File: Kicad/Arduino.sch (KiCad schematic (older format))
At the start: 5 parts

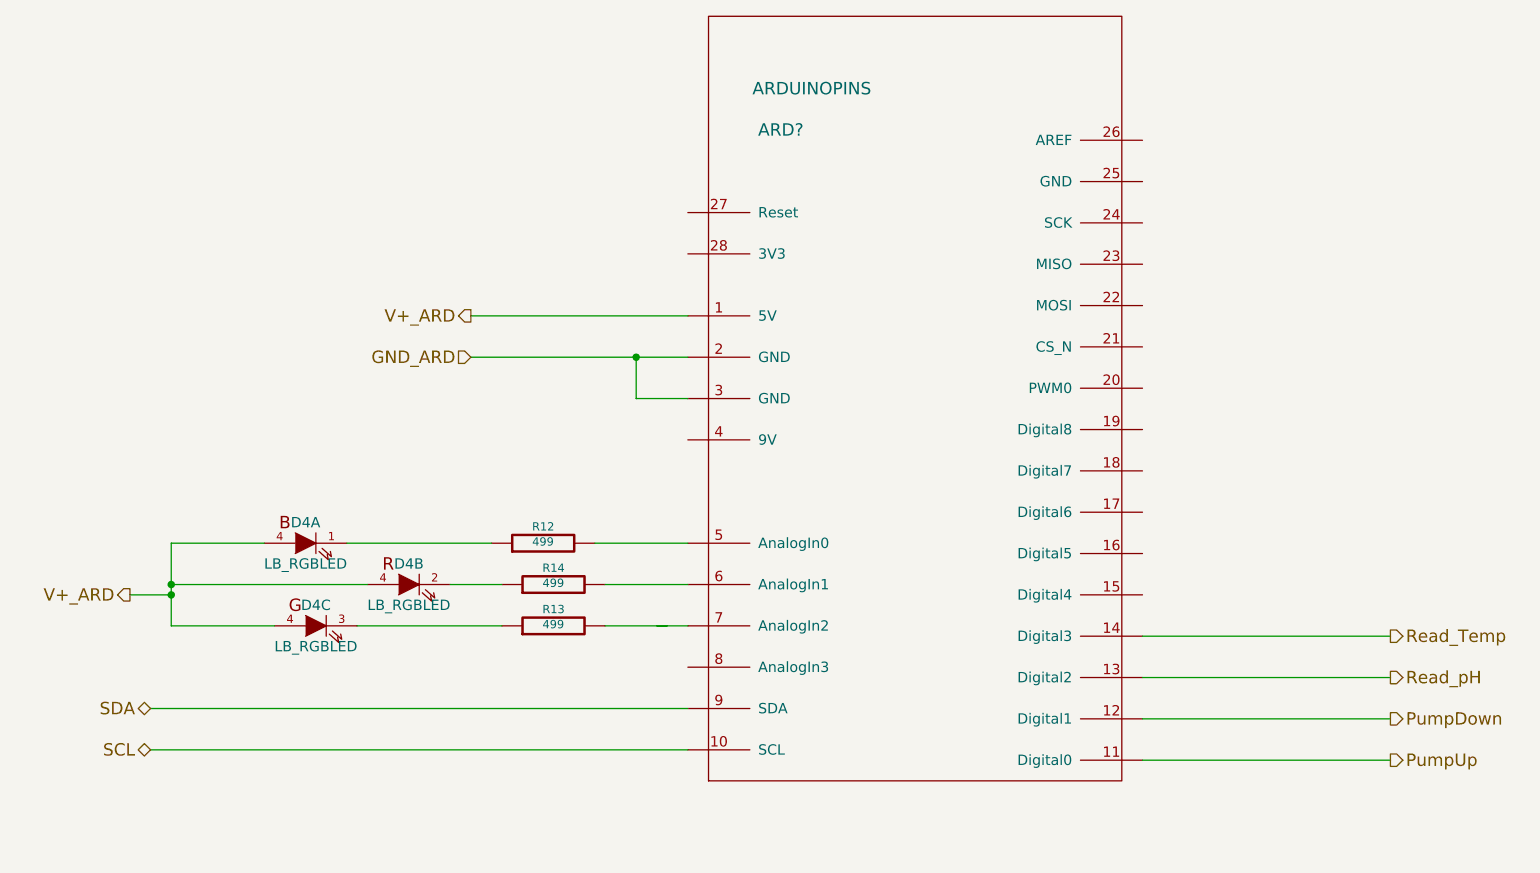
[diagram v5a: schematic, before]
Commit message: prior to using Arduino ADC
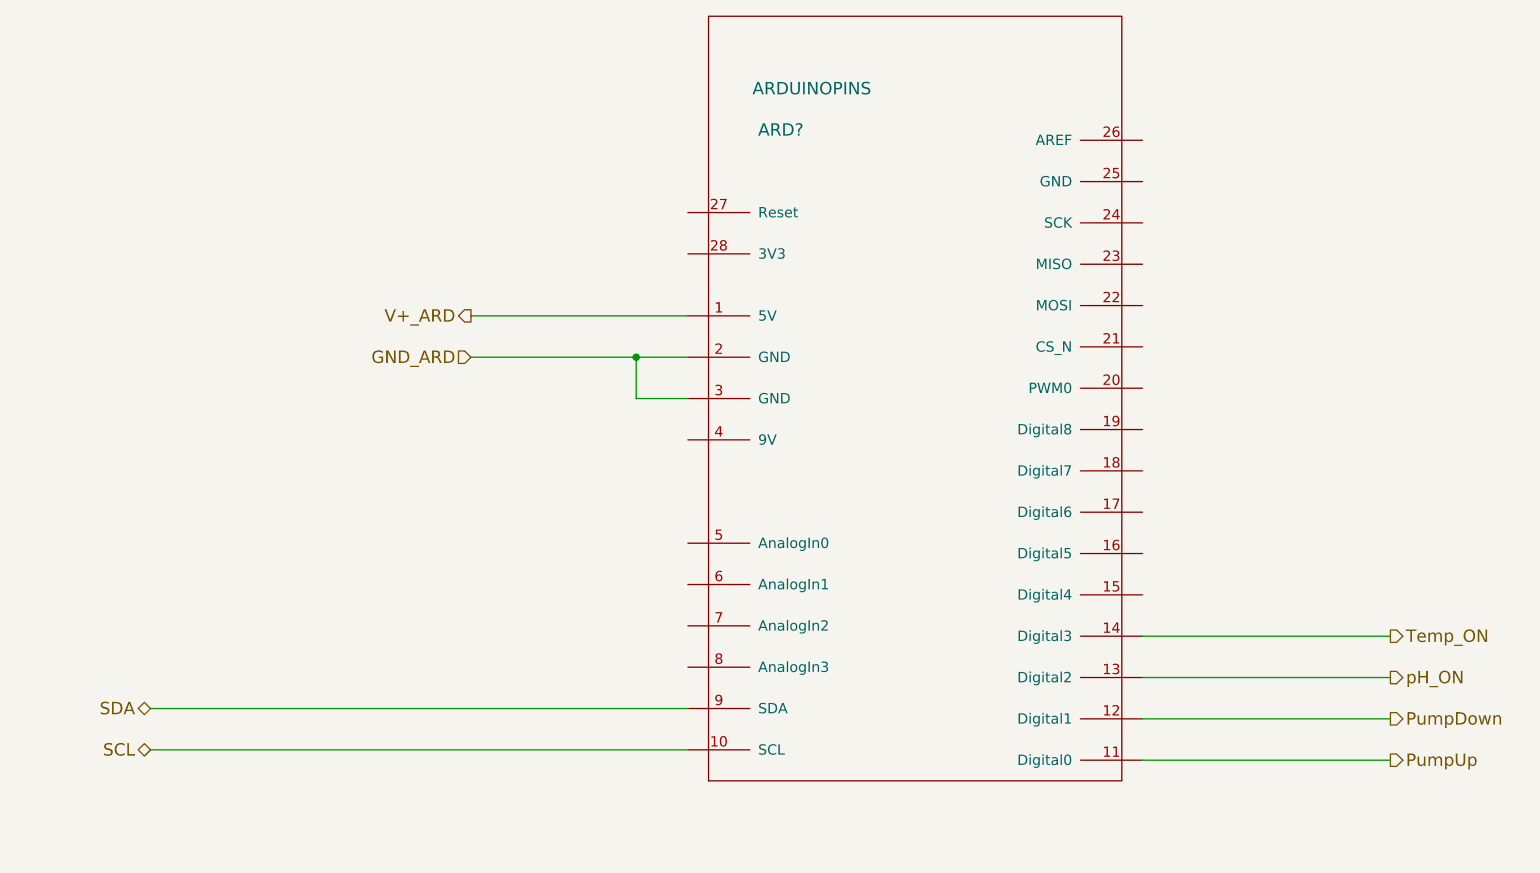
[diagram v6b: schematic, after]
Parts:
- removed D4: LB_RGBLED, ~, symbol LB_RGBLED
- removed R12, R13, R14: 499, ~, symbol R
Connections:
- net labels added: Temp_ON, pH_ON
- net labels removed: Read_Temp, Read_pH
- wire segments 22 -> 10
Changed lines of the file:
@@
 $Descr A4 11693 8268
 encoding utf-8
-Sheet 6 7
+Sheet 5 7
 Title ""
-Date "11 nov 2014"
+Date "12 nov 2014"
 Rev ""
 Comp ""
@@
 Text HLabel 6950 4600 2    60   Output ~ 0
 PumpUp
-$Comp
-L R R14
-U 1 1 540F4E5D
-P 2900 3750
-F 0 "R14" V 2980 3750 40  0000 C CNN
-F 1 "499" V 2907 3751 40  0000 C CNN
-F 2 "~" V 2830 3750 30  0000 C CNN
-F 3 "~" H 2900 3750 30  0000 C CNN
-	1    2900 3750
-	0    -1   -1   0
-$EndComp
-$Comp
-L R R13
-U 1 1 540F4E9E
-P 2900 3950
-F 0 "R13" V 2980 3950 40  0000 C CNN
-F 1 "499" V 2907 3951 40  0000 C CNN
-F 2 "~" V 2830 3950 30  0000 C CNN
-F 3 "~" H 2900 3950 30  0000 C CNN
-	1    2900 3950
-	0    -1   -1   0
-$EndComp
-$Comp
-L R R12
-U 1 1 540F4F03
-P 2850 3550
-F 0 "R12" V 2930 3550 40  0000 C CNN
-F 1 "499" V 2857 3551 40  0000 C CNN
-F 2 "~" V 2780 3550 30  0000 C CNN
-F 3 "~" H 2850 3550 30  0000 C CNN
-	1    2850 3550
-	0    -1   -1   0
-$EndComp
-Wire Wire Line
-	3550 3550 3100 3550
-Wire Wire Line
-	1900 3550 2600 3550
-Wire Wire Line
-	1950 3950 2650 3950
-Text HLabel 850  3800 0    60   Output ~ 0
-V+_ARD
-$Comp
-L LB_RGBLED D4
-U 1 1 544128B0
-P 1700 3550
-F 0 "D4" H 1700 3650 50  0000 C CNN
-F 1 "LB_RGBLED" H 1700 3450 50  0000 C CNN
-F 2 "~" H 1700 3550 60  0000 C CNN
-F 3 "~" H 1700 3550 60  0000 C CNN
-	1    1700 3550
-	1    0    0    -1
-$EndComp
-$Comp
-L LB_RGBLED D4
-U 2 1 544128BD
-P 2200 3750
-F 0 "D4" H 2200 3850 50  0000 C CNN
-F 1 "LB_RGBLED" H 2200 3650 50  0000 C CNN
-F 2 "~" H 2200 3750 60  0000 C CNN
-F 3 "~" H 2200 3750 60  0000 C CNN
-	2    2200 3750
-	1    0    0    -1
-$EndComp
-$Comp
-L LB_RGBLED D4
-U 3 1 544128C3
-P 1750 3950
-F 0 "D4" H 1750 4050 50  0000 C CNN
-F 1 "LB_RGBLED" H 1750 3850 50  0000 C CNN
-F 2 "~" H 1750 3950 60  0000 C CNN
-F 3 "~" H 1750 3950 60  0000 C CNN
-	3    1750 3950
-	1    0    0    -1
-$EndComp
-Wire Wire Line
-	1050 3550 1500 3550
-Wire Wire Line
-	1050 3950 1550 3950
 Wire Wire Line
 	3550 2850 3300 2850
@@
 	3300 2850 3300 2650
 Connection ~ 3300 2650
-Wire Wire Line
-	3450 3950 3150 3950
-Wire Wire Line
-	3150 3750 3550 3750
-Wire Wire Line
-	3400 3950 3550 3950
 $Comp
 L ARDUINOPINS ARD?
@@
 Wire Wire Line
 	6950 4400 5750 4400
-Wire Wire Line
-	2650 3750 2400 3750
-Wire Wire Line
-	2000 3750 1050 3750
-Wire Wire Line
-	1050 3550 1050 3950
-Connection ~ 1050 3750
 Text HLabel 950  4350 0    60   BiDi ~ 0
 SDA
@@
 SCL
 Text HLabel 6950 4200 2    60   Output ~ 0
-Read_pH
+pH_ON
 Wire Wire Line
 	5750 4200 6950 4200
 Text HLabel 6950 4000 2    60   Output ~ 0
-Read_Temp
+Temp_ON
 Wire Wire Line
 	5750 4000 6950 4000
-Wire Wire Line
-	850  3800 1050 3800
-Connection ~ 1050 3800
 $EndSCHEMATC
